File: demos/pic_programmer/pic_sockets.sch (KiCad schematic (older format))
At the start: 7 parts, among them P2 SUPP28, P3 SUPP40, U1 24Cxx, U5 PIC_18_PINS, U6 PIC_8_PINS

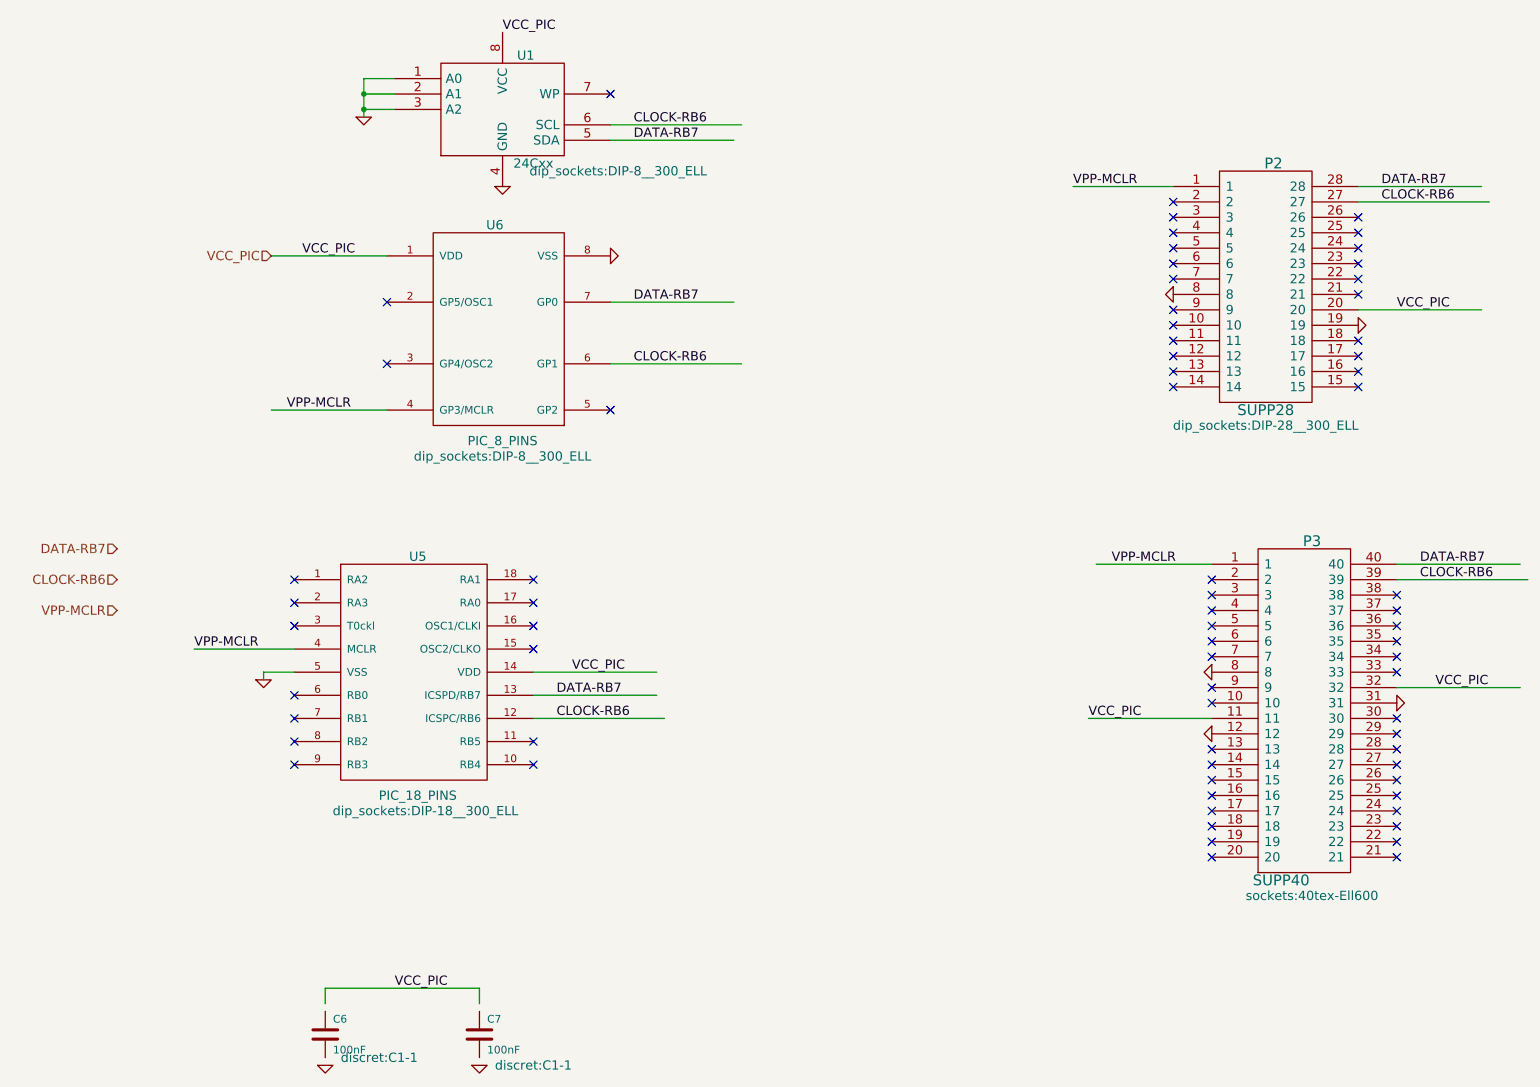
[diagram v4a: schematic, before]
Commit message: demos/ schematic tidying
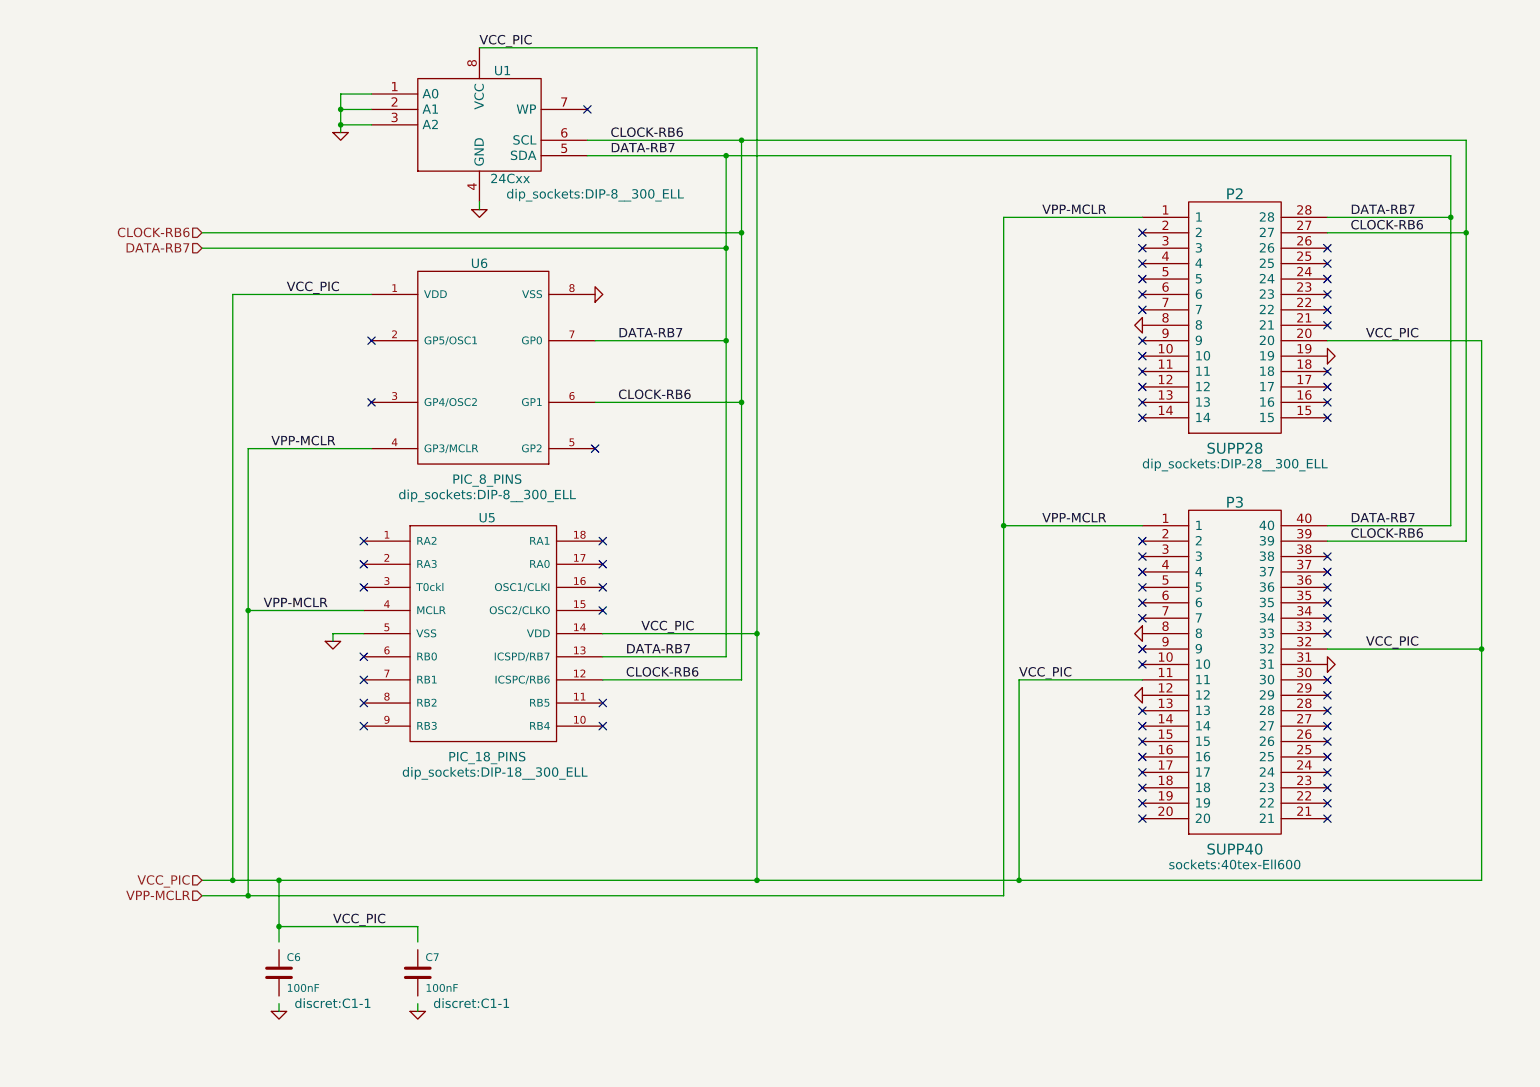
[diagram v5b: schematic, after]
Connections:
- wire segments 28 -> 46
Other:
- moved on the sheet: C6, C7, P2, P3, U1, U5, U6

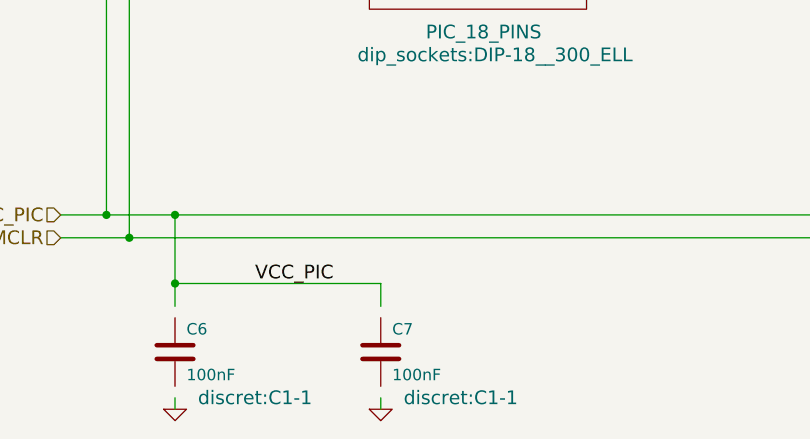
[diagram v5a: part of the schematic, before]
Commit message: Demos: make a private library for each demo, to avoid issues when using modified kicad new schematic libraries
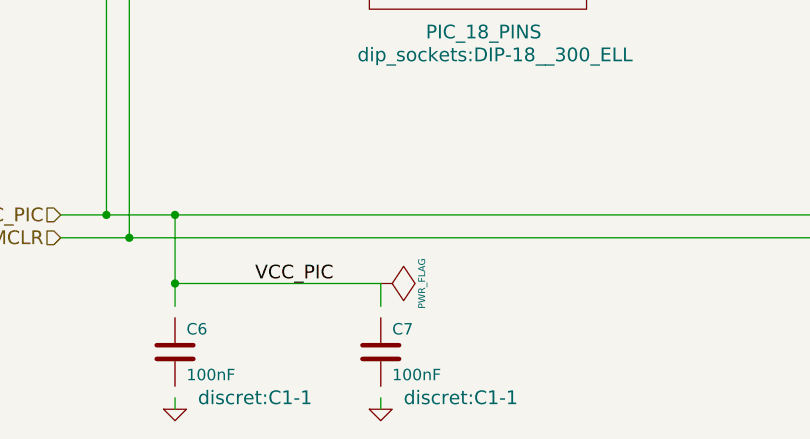
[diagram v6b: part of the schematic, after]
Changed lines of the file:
@@
 EESchema Schematic File Version 2
+LIBS:pic_programmer_schlib
 LIBS:power
-LIBS:device
-LIBS:74xx
-LIBS:conn
-LIBS:xilinx
 LIBS:pic_programmer-cache
 EELAYER 25 0
@@
 Wire Wire Line
 	3300 7000 3300 7050
+$Comp
+L PWR_FLAG #FLG047
+U 1 1 5558FA28
+P 3300 6500
+F 0 "#FLG047" H 3300 6595 30  0001 C CNN
+F 1 "PWR_FLAG" H 3300 6680 30  0000 C CNN
+F 2 "" H 3300 6500 60  0000 C CNN
+F 3 "" H 3300 6500 60  0000 C CNN
+	1    3300 6500
+	0    1    1    0
+$EndComp
 $EndSCHEMATC

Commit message: merge from production bzr6934 to bzr 6953
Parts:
- C6, C7: footprint discret:C1-1 -> Discret:C1-1
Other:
- moved on the sheet: C6, C7
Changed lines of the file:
@@
 EESchema Schematic File Version 2
+LIBS:device
 LIBS:pic_programmer_schlib
 LIBS:power
@@
 L GND #PWR040
 U 1 1 442AA147
-P 3300 7050
-F 0 "#PWR040" H 3300 7050 30  0001 C CNN
-F 1 "GND" H 3300 6980 30  0001 C CNN
-F 2 "" H 3300 7050 60  0001 C CNN
-F 3 "" H 3300 7050 60  0001 C CNN
-	1    3300 7050
+P 3300 6950
+F 0 "#PWR040" H 3300 6950 30  0001 C CNN
+F 1 "GND" H 3300 6880 30  0001 C CNN
+F 2 "" H 3300 6950 60  0001 C CNN
+F 3 "" H 3300 6950 60  0001 C CNN
+	1    3300 6950
 	1    0    0    -1
 $EndComp
@@
 L C C7
 U 1 1 442AA145
-P 3300 6800
-F 0 "C7" H 3350 6900 50  0000 L CNN
-F 1 "100nF" H 3350 6700 50  0000 L CNN
-F 2 "discret:C1-1" H 3650 6600 60  0000 C CNN
-F 3 "" H 3300 6800 60  0001 C CNN
-	1    3300 6800
+P 3300 6750
+F 0 "C7" H 3350 6850 50  0000 L CNN
+F 1 "100nF" H 3350 6650 50  0000 L CNN
+F 2 "Discret:C1-1" H 3500 6600 30  0000 C CNN
+F 3 "" H 3300 6750 60  0001 C CNN
+	1    3300 6750
 	1    0    0    -1
 $EndComp
@@
 L GND #PWR041
 U 1 1 442AA138
-P 2400 7050
-F 0 "#PWR041" H 2400 7050 30  0001 C CNN
-F 1 "GND" H 2400 6980 30  0001 C CNN
-F 2 "" H 2400 7050 60  0001 C CNN
-F 3 "" H 2400 7050 60  0001 C CNN
-	1    2400 7050
+P 2400 6950
+F 0 "#PWR041" H 2400 6950 30  0001 C CNN
+F 1 "GND" H 2400 6880 30  0001 C CNN
+F 2 "" H 2400 6950 60  0001 C CNN
+F 3 "" H 2400 6950 60  0001 C CNN
+	1    2400 6950
 	1    0    0    -1
 $EndComp
@@
 L C C6
 U 1 1 442AA12B
-P 2400 6800
-F 0 "C6" H 2450 6900 50  0000 L CNN
-F 1 "100nF" H 2450 6700 50  0000 L CNN
-F 2 "discret:C1-1" H 2750 6600 60  0000 C CNN
-F 3 "" H 2400 6800 60  0001 C CNN
-	1    2400 6800
+P 2400 6750
+F 0 "C6" H 2450 6850 50  0000 L CNN
+F 1 "100nF" H 2450 6650 50  0000 L CNN
+F 2 "Discret:C1-1" H 2600 6600 30  0000 C CNN
+F 3 "" H 2400 6750 60  0001 C CNN
+	1    2400 6750
 	1    0    0    -1
 $EndComp
@@
 	3700 1850 3700 1800
 Wire Wire Line
-	2400 7000 2400 7050
-Wire Wire Line
-	3300 7000 3300 7050
+	2400 6900 2400 6950
+Wire Wire Line
+	3300 6900 3300 6950
 $Comp
 L PWR_FLAG #FLG047
